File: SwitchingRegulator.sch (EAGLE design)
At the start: 35 parts, among them J1 APP_2POS_CONFIG5V_HORIZ, J2 APP_2POS_CONFIG5V_HORIZ, J4 APP_2POS_CONFIG12V_HORIZ, U1 OKI-78SR-5/1.5-W36HC

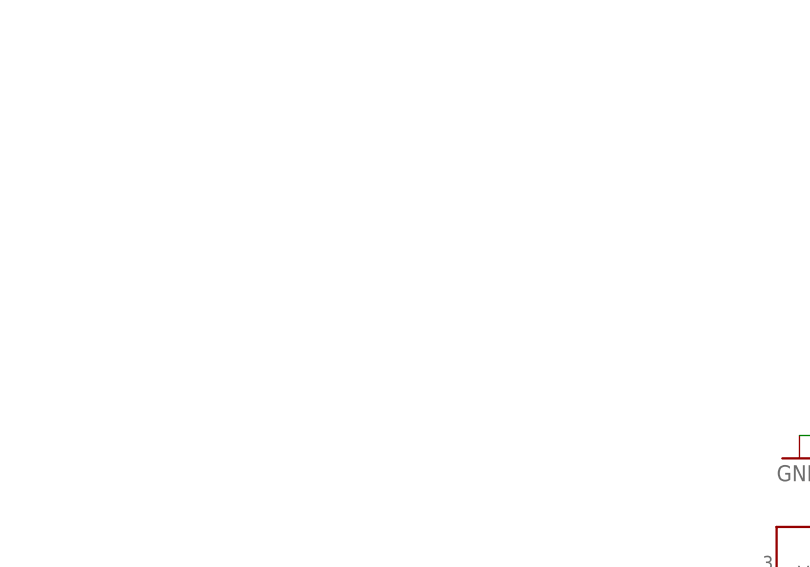
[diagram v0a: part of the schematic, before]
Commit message: Heatsinks added, rearranges needed
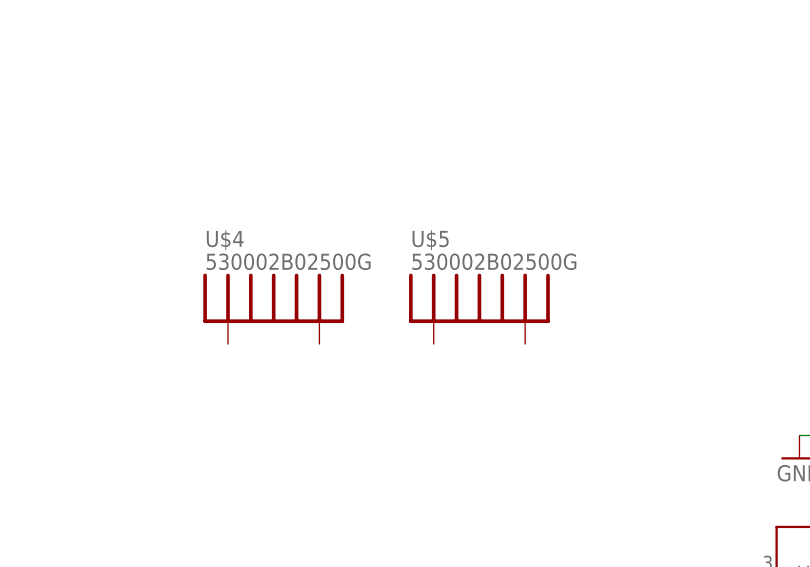
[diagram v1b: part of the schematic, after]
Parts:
- added U$4, U$5: 530002B02500G, buckconverter:530002B02500G
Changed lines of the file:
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@@
 <part name="RC2" library="SparkFun-Passives" deviceset="RESISTOR" device="0603-RES" value="10k"/>
 <part name="RF" library="SparkFun-Passives" deviceset="RESISTOR" device="0603-RES" value="10"/>
-<part name="GND1" library="SparkFun-Aesthetics" deviceset="GND" device=""/>
-<part name="GND3" library="SparkFun-Aesthetics" deviceset="GND" device=""/>
-<part name="GND4" library="SparkFun-Aesthetics" deviceset="GND" device=""/>
-<part name="GND5" library="SparkFun-Aesthetics" deviceset="GND" device=""/>
+<part name="GND1" library="SparkFun-Aesthetics" library_urn="urn:adsk.eagle:library:507" deviceset="GND" device=""/>
+<part name="GND3" library="SparkFun-Aesthetics" library_urn="urn:adsk.eagle:library:507" deviceset="GND" device=""/>
+<part name="GND4" library="SparkFun-Aesthetics" library_urn="urn:adsk.eagle:library:507" deviceset="GND" device=""/>
+<part name="GND5" library="SparkFun-Aesthetics" library_urn="urn:adsk.eagle:library:507" deviceset="GND" device=""/>
 <part name="J1" library="MRDT-Connectors" deviceset="APP_2POS_CONFIG" device="5V_HORIZ"/>
 <part name="J2" library="MRDT-Connectors" deviceset="APP_2POS_CONFIG" device="5V_HORIZ"/>
 <part name="C1" library="buckconverter" deviceset="UCZ1K220MCL1GS" device="" value="22u"/>
-<part name="GND2" library="SparkFun-PowerSymbols" deviceset="GND" device=""/>
+<part name="GND2" library="SparkFun-PowerSymbols" library_urn="urn:adsk.eagle:library:530" deviceset="GND" device=""/>
 <part name="L1" library="buckconverter" deviceset="PQ3218-3R3-70-T" device="" value="3.3uH"/>
 <part name="COUT1" library="buckconverter" deviceset="EGPD101ELL221MK25H" device="" value="220u"/>
@@
 <part name="CDRVCC" library="SparkFun-Passives" deviceset="CAP" device="0603-CAP" value="10u"/>
 <part name="J4" library="MRDT-Connectors" deviceset="APP_2POS_CONFIG" device="12V_HORIZ"/>
-<part name="GND6" library="SparkFun-Aesthetics" deviceset="GND" device=""/>
-<part name="GND7" library="SparkFun-Aesthetics" deviceset="GND" device=""/>
-<part name="GND8" library="SparkFun-Aesthetics" deviceset="GND" device=""/>
-<part name="GND9" library="SparkFun-Aesthetics" deviceset="GND" device=""/>
-<part name="GND10" library="SparkFun-Aesthetics" deviceset="GND" device=""/>
+<part name="GND6" library="SparkFun-Aesthetics" library_urn="urn:adsk.eagle:library:507" deviceset="GND" device=""/>
+<part name="GND7" library="SparkFun-Aesthetics" library_urn="urn:adsk.eagle:library:507" deviceset="GND" device=""/>
+<part name="GND8" library="SparkFun-Aesthetics" library_urn="urn:adsk.eagle:library:507" deviceset="GND" device=""/>
+<part name="GND9" library="SparkFun-Aesthetics" library_urn="urn:adsk.eagle:library:507" deviceset="GND" device=""/>
+<part name="GND10" library="SparkFun-Aesthetics" library_urn="urn:adsk.eagle:library:507" deviceset="GND" device=""/>
 <part name="H1" library="MRDT-Hardware" deviceset="MOUNTING_HOLE" device="#8"/>
 <part name="H2" library="MRDT-Hardware" deviceset="MOUNTING_HOLE" device="#8"/>
@@
 <part name="U$2" library="buckconverter" deviceset="IPP052N06L3GXKSA1" device=""/>
 <part name="U$3" library="buckconverter" deviceset="IPP052N06L3GXKSA1" device=""/>
+<part name="U$4" library="buckconverter" deviceset="530002B02500G" device=""/>
+<part name="U$5" library="buckconverter" deviceset="530002B02500G" device=""/>
 </parts>
 <sheets>
@@
 <instance part="U$2" gate="G$1" x="152.4" y="132.08"/>
 <instance part="U$3" gate="G$1" x="152.4" y="109.22"/>
+<instance part="U$4" gate="G$1" x="58.42" y="200.66"/>
+<instance part="U$5" gate="G$1" x="81.28" y="200.66"/>
 </instances>
 <busses>
@@
 which will not be processed correctly with this version.
 </note>
+<note version="8.2" severity="warning">
+Since Version 8.2, EAGLE supports online libraries. The ids
+of those online libraries will not be understood (or retained)
+with this version.
+</note>
+<note version="8.3" severity="warning">
+Since Version 8.3, EAGLE supports URNs for individual library
+assets (packages, symbols, and devices). The URNs of those assets
+will not be understood (or retained) with this version.
+</note>
 </compatibility>
